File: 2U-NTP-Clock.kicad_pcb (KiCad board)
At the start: 2 copper layers, 482.6 x 83.8 mm, 279 parts, among them J1 Barrel_Jack_Switch, J2 Conn_01x06_Socket, Q1 BSS138, Q10 BSS138, Q11 BSS138, Q12 BSS138, Q13 BSS138, Q14 BSS138, Q15 BSS138, Q16 BSS138, Q17 BSS138, Q18 BSS138, Q19 BSS138, Q2 BSS138, Q20 BSS138, Q21 BSS138, Q22 BSS138, Q23 BSS138, Q24 BSS138, Q25 BSS138, Q26 BSS138, Q27 BSS138, Q28 BSS138, Q29 BSS138, Q3 BSS138, Q30 BSS138, Q31 BSS138, Q32 BSS138, Q33 BSS138, Q34 BSS138, Q35 BSS138, Q36 BSS138, Q37 BSS138, Q38 BSS138, Q39 BSS138, Q4 BSS138, Q40 BSS138, Q41 BSS138, Q42 BSS138, Q43 BSS138, Q5 BSS138, Q6 BSS138, Q7 BSS138, Q8 BSS138, Q9 BSS138, SW1 SW_Push, SW2 SW_Push, SW3 SW_Push, SW4 SW_Push, SW5 SW_Push, SW6 SW_Slide_DPDT, U3 74HC595, U4 74HC595, U5 74HC595, U6 74HC595, U7 74HC595, U8 74HC595, U9 L7805

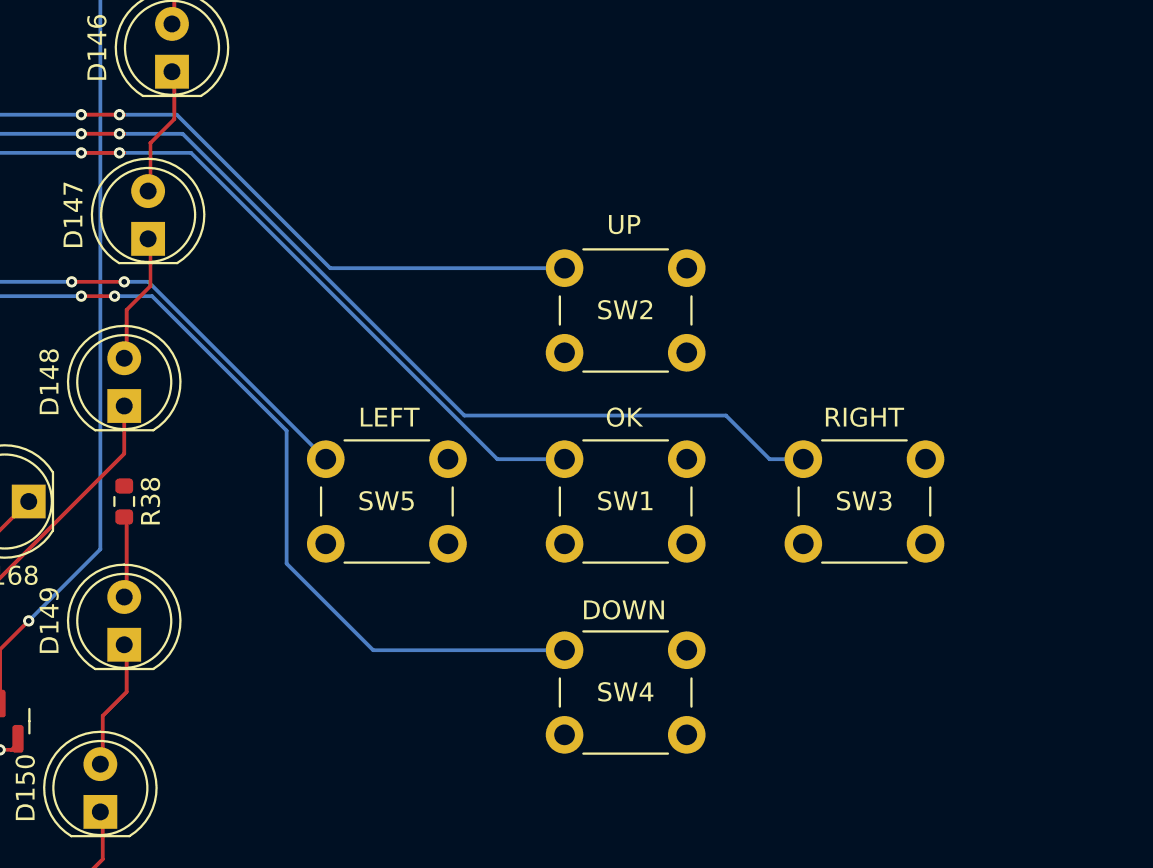
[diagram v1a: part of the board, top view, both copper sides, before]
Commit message: 操作用スイッチを移設
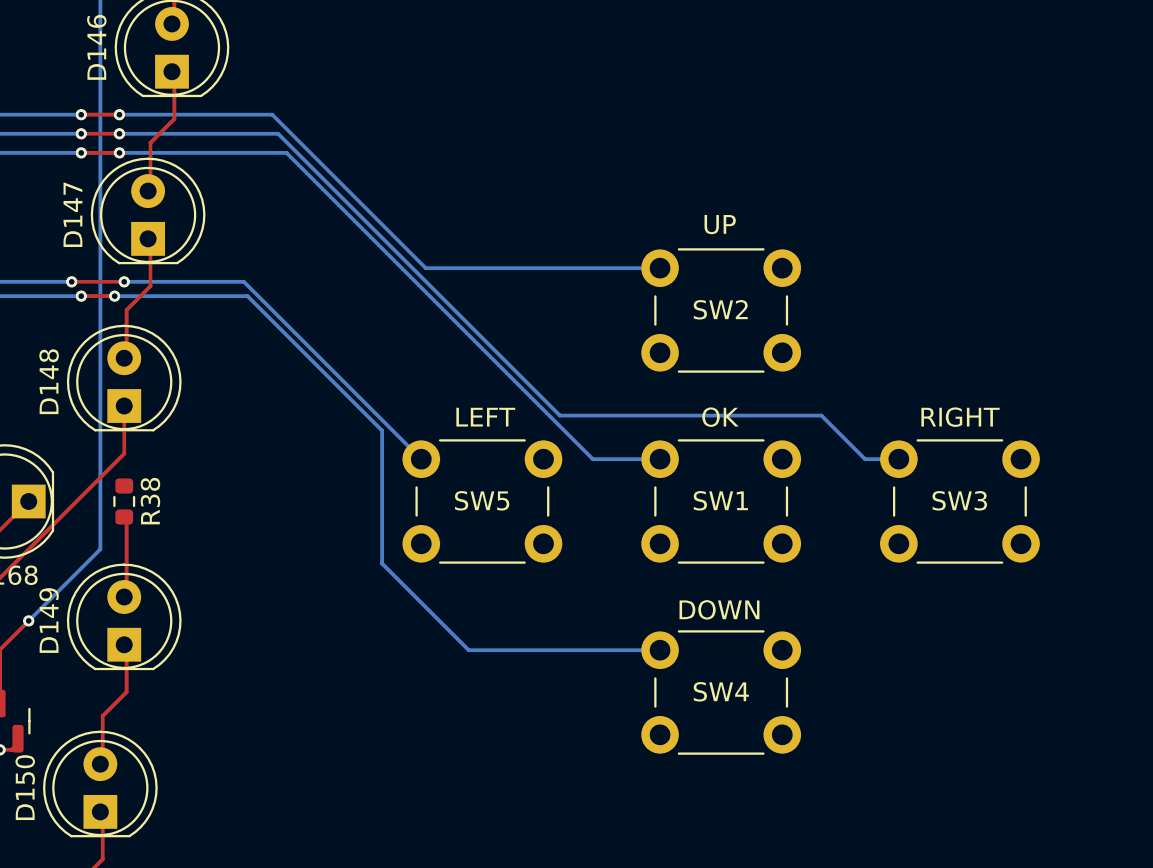
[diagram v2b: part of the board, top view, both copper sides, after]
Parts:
- moved SW1 5.08 mm to (499.7, 200.9)
- moved SW2 5.08 mm to (499.7, 190.8)
- moved SW4 5.08 mm to (499.7, 211.1)
- moved SW5 5.08 mm to (487.0, 200.9)
- moved SW3 5.08 mm to (512.4, 200.9)
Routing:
- net /UP: track 434.6 -> 439.7 mm
- net /RIGHT: track 449.6 -> 454.7 mm
- net /OK: track 434.9 -> 440.0 mm
- net /LEFT: track 404.9 -> 410.0 mm
- net /DOWN: track 421.8 -> 426.9 mm
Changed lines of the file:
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@@
 	(footprint "Button_Switch_THT:SW_PUSH_6mm"
 		(layer "F.Cu")
-		(at 481.89 200.95)
+		(at 486.97 200.95)
 		(descr "Generic 6mm SW tactile push button")
 		(tags "tact sw push 6mm")
@@
 	(footprint "Button_Switch_THT:SW_PUSH_6mm"
 		(layer "F.Cu")
-		(at 494.59 200.95)
+		(at 499.67 200.95)
 		(descr "Generic 6mm SW tactile push button")
 		(tags "tact sw push 6mm")
@@
 	(footprint "Button_Switch_THT:SW_PUSH_6mm"
 		(layer "F.Cu")
-		(at 494.59 190.79)
+		(at 499.67 190.79)
 		(descr "Generic 6mm SW tactile push button")
 		(tags "tact sw push 6mm")
@@
 	(footprint "Button_Switch_THT:SW_PUSH_6mm"
 		(layer "F.Cu")
-		(at 507.29 200.95)
+		(at 512.37 200.95)
 		(descr "Generic 6mm SW tactile push button")
 		(tags "tact sw push 6mm")
@@
 	(footprint "Button_Switch_THT:SW_PUSH_6mm"
 		(layer "F.Cu")
-		(at 494.59 211.11)
+		(at 499.67 211.11)
 		(descr "Generic 6mm SW tactile push button")
 		(tags "tact sw push 6mm")
@@
 	)
 	(gr_text "LEFT"
-		(at 485.25 198.75 0)
+		(at 490.33 198.75 0)
 		(layer "F.SilkS")
 		(effects
@@
 	)
 	(gr_text "DOWN"
-		(at 497.75 209 0)
+		(at 502.83 209 0)
 		(layer "F.SilkS")
 		(effects
@@
 	)
 	(gr_text "UP"
-		(at 497.75 188.5 0)
+		(at 502.83 188.5 0)
 		(layer "F.SilkS")
 		(effects
@@
 	)
 	(gr_text "OK"
-		(at 497.75 198.75 0)
+		(at 502.83 198.75 0)
 		(layer "F.SilkS")
 		(effects
@@
 	)
 	(gr_text "RIGHT"
-		(at 510.5 198.75 0)
+		(at 515.58 198.75 0)
 		(layer "F.SilkS")
 		(effects
@@
 	)
 	(segment
+		(start 479.806 184.658)
+		(end 496.098 200.95)
+		(width 0.2)
+		(layer "B.Cu")
+		(net 3)
+	)
+	(segment
 		(start 348.234 184.658)
 		(end 298.45 184.658)
@@
 	)
 	(segment
-		(start 474.726 184.658)
-		(end 471.17 184.658)
+		(start 471.17 184.658)
+		(end 479.806 184.658)
 		(width 0.2)
 		(layer "B.Cu")
@@
 	)
 	(segment
-		(start 491.018 200.95)
-		(end 474.726 184.658)
+		(start 247.396 181.102)
+		(end 242.824 181.102)
 		(width 0.2)
 		(layer "B.Cu")
@@
 	)
 	(segment
-		(start 247.396 181.102)
-		(end 242.824 181.102)
+		(start 104.902 221.234)
+		(end 104.902 218.636314)
 		(width 0.2)
 		(layer "B.Cu")
@@
 	)
 	(segment
-		(start 104.902 221.234)
-		(end 104.902 218.636314)
+		(start 496.098 200.95)
+		(end 499.67 200.95)
 		(width 0.2)
 		(layer "B.Cu")
@@
 	)
 	(segment
-		(start 494.59 200.95)
-		(end 491.018 200.95)
-		(width 0.2)
-		(layer "B.Cu")
-		(net 3)
-	)
-	(segment
 		(start 104.902 218.636314)
 		(end 106.622314 216.916)
@@
 	)
 	(segment
-		(start 473.964 182.626)
-		(end 471.17 182.626)
-		(width 0.2)
-		(layer "B.Cu")
-		(net 5)
-	)
-	(segment
 		(start 129.794 213.106)
 		(end 127 215.9)
@@
 	)
 	(segment
-		(start 494.59 190.79)
-		(end 482.128 190.79)
+		(start 471.17 182.626)
+		(end 479.044 182.626)
 		(width 0.2)
 		(layer "B.Cu")
@@
 	)
 	(segment
+		(start 487.208 190.79)
+		(end 499.67 190.79)
+		(width 0.2)
+		(layer "B.Cu")
+		(net 5)
+	)
+	(segment
 		(start 468.884 182.626)
 		(end 419.1 182.626)
@@
 	)
 	(segment
-		(start 482.128 190.79)
-		(end 473.964 182.626)
+		(start 479.044 182.626)
+		(end 487.208 190.79)
 		(width 0.2)
 		(layer "B.Cu")
@@
 	)
 	(segment
-		(start 507.29 200.95)
-		(end 505.496 200.95)
+		(start 510.576 200.95)
+		(end 512.37 200.95)
 		(width 0.2)
 		(layer "B.Cu")
@@
 	)
 	(segment
-		(start 104.502 218.332)
-		(end 104.502 222.104)
+		(start 508.254 198.628)
+		(end 510.576 200.95)
 		(width 0.2)
 		(layer "B.Cu")
@@
 	)
 	(segment
-		(start 505.496 200.95)
-		(end 503.174 198.628)
+		(start 104.502 218.332)
+		(end 104.502 222.104)
 		(width 0.2)
 		(layer "B.Cu")
@@
 	)
 	(segment
-		(start 503.174 198.628)
-		(end 489.261686 198.628)
+		(start 479.355686 183.642)
+		(end 494.341686 198.628)
 		(width 0.2)
 		(layer "B.Cu")
@@
 	)
 	(segment
-		(start 474.275686 183.642)
-		(end 471.17 183.642)
+		(start 358.648 183.642)
+		(end 350.52 183.642)
 		(width 0.2)
 		(layer "B.Cu")
@@
 	)
 	(segment
-		(start 358.648 183.642)
-		(end 350.52 183.642)
+		(start 130.302 189.992)
+		(end 130.302 213.36)
 		(width 0.2)
 		(layer "B.Cu")
@@
 	)
 	(segment
-		(start 489.261686 198.628)
-		(end 474.275686 183.642)
+		(start 468.884 183.642)
+		(end 419.1 183.642)
 		(width 0.2)
 		(layer "B.Cu")
@@
 	)
 	(segment
-		(start 130.302 189.992)
-		(end 130.302 213.36)
+		(start 471.17 183.642)
+		(end 479.355686 183.642)
 		(width 0.2)
 		(layer "B.Cu")
@@
 	)
 	(segment
-		(start 468.884 183.642)
-		(end 419.1 183.642)
+		(start 247.904 180.594)
+		(end 242.316 180.594)
 		(width 0.2)
 		(layer "B.Cu")
@@
 	)
 	(segment
-		(start 247.904 180.594)
-		(end 242.316 180.594)
+		(start 494.341686 198.628)
+		(end 508.254 198.628)
 		(width 0.2)
 		(layer "B.Cu")
@@
 	)
 	(segment
-		(start 484.414 211.11)
-		(end 479.806 206.502)
-		(width 0.2)
-		(layer "B.Cu")
-		(net 17)
-	)
-	(segment
 		(start 229.362 192.278)
 		(end 296.164 192.278)
@@
 	)
 	(segment
-		(start 131.826 197.104)
-		(end 136.652 192.278)
+		(start 470.662 192.278)
+		(end 477.732314 192.278)
 		(width 0.2)
 		(layer "B.Cu")
@@
 	)
 	(segment
-		(start 494.59 211.11)
-		(end 484.414 211.11)
+		(start 131.826 197.104)
+		(end 136.652 192.278)
 		(width 0.2)
 		(layer "B.Cu")
@@
 	)
 	(segment
-		(start 472.652314 192.278)
-		(end 470.662 192.278)
+		(start 484.886 199.431686)
+		(end 484.886 206.502)
 		(width 0.2)
 		(layer "B.Cu")
@@
 	)
 	(segment
-		(start 479.806 206.502)
-		(end 479.806 199.431686)
+		(start 477.732314 192.278)
+		(end 484.886 199.431686)
 		(width 0.2)
 		(layer "B.Cu")
@@
 	)
 	(segment
-		(start 479.806 199.431686)
-		(end 472.652314 192.278)
+		(start 489.494 211.11)
+		(end 499.67 211.11)
+		(width 0.2)
+		(layer "B.Cu")
+		(net 17)
+	)
+	(segment
+		(start 484.886 206.502)
+		(end 489.494 211.11)
 		(width 0.2)
 		(layer "B.Cu")
@@
 	)
 	(segment
-		(start 472.456 191.516)
-		(end 471.17 191.516)
+		(start 477.536 191.516)
+		(end 486.97 200.95)
 		(width 0.2)
 		(layer "B.Cu")
@@
 	)
 	(segment
-		(start 481.89 200.95)
-		(end 472.456 191.516)
+		(start 471.17 191.516)
+		(end 477.536 191.516)
 		(width 0.2)
 		(layer "B.Cu")

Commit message: 基板配線修正
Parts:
- moved R43 64.5 mm to (364.5, 164.1), turned to -90 degrees
- moved D170 40.6 mm to (364.5, 223.5), turned to 90 degrees
- moved D169 35.6 mm to (364.5, 185.4), turned to 90 degrees
- moved Q43 13.2 mm to (245.1, 241.8)
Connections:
- D103 pad 2: Net-(D102-K) -> Net-(D101-A)
- D104 pad 1: Net-(D104-K) -> Net-(D102-K)
- D107 pad 2: Net-(D106-K) -> Net-(D105-A)
- D108 pad 1: Net-(D108-K) -> Net-(D106-K)
- D11 pad 2: Net-(D10-K) -> Net-(D11-A)
- D111 pad 2: Net-(D110-K) -> Net-(D109-A)
- D112 pad 1: Net-(D112-K) -> Net-(D110-K)
- D115 pad 2: Net-(D114-K) -> Net-(D113-A)
- D116 pad 1: Net-(D116-K) -> Net-(D114-K)
- D119 pad 2: Net-(D118-K) -> Net-(D117-A)
- D12 pad 1: Net-(D12-K) -> Net-(D10-K)
- D120 pad 1: Net-(D120-K) -> Net-(D118-K)
- D123 pad 2: Net-(D122-K) -> Net-(D121-A)
- D124 pad 1: Net-(D124-K) -> Net-(D122-K)
- D127 pad 2: Net-(D126-K) -> Net-(D125-A)
- D128 pad 1: Net-(D128-K) -> Net-(D126-K)
- D131 pad 2: Net-(D130-K) -> Net-(D129-A)
- D132 pad 1: Net-(D132-K) -> Net-(D130-K)
- D135 pad 2: Net-(D134-K) -> Net-(D133-A)
- D136 pad 1: Net-(D136-K) -> Net-(D134-K)
- D139 pad 2: Net-(D138-K) -> Net-(D137-A)
- D140 pad 1: Net-(D140-K) -> Net-(D138-K)
- D143 pad 2: Net-(D142-K) -> Net-(D141-A)
- D144 pad 1: Net-(D144-K) -> Net-(D142-K)
- D147 pad 2: Net-(D146-K) -> Net-(D145-A)
- D148 pad 1: Net-(D148-K) -> Net-(D146-K)
- D15 pad 2: Net-(D14-K) -> Net-(D13-A)
- D151 pad 2: Net-(D150-K) -> Net-(D149-A)
- D152 pad 1: Net-(D152-K) -> Net-(D150-K)
- D155 pad 2: Net-(D154-K) -> Net-(D153-A)
- D156 pad 1: Net-(D156-K) -> Net-(D154-K)
- D159 pad 2: Net-(D158-K) -> Net-(D157-A)
- D16 pad 1: Net-(D16-K) -> Net-(D14-K)
- D160 pad 1: Net-(D160-K) -> Net-(D158-K)
- D163 pad 2: Net-(D162-K) -> Net-(D161-A)
- D164 pad 1: Net-(D164-K) -> Net-(D162-K)
- D167 pad 2: Net-(D166-K) -> Net-(D165-A)
- D168 pad 1: Net-(D168-K) -> Net-(D166-K)
- D171 pad 2: Net-(D170-K) -> Net-(D169-A)
- D172 pad 1: Net-(D172-K) -> Net-(D170-K)
- D19 pad 2: Net-(D18-K) -> Net-(D17-A)
- D20 pad 1: Net-(D20-K) -> Net-(D18-K)
- D23 pad 2: Net-(D22-K) -> Net-(D21-A)
- D24 pad 1: Net-(D24-K) -> Net-(D22-K)
- D27 pad 2: Net-(D26-K) -> Net-(D25-A)
- D28 pad 1: Net-(D28-K) -> Net-(D26-K)
- D3 pad 2: Net-(D2-K) -> Net-(D1-A)
- D31 pad 2: Net-(D30-K) -> Net-(D29-A)
- D32 pad 1: Net-(D32-K) -> Net-(D30-K)
- D35 pad 2: Net-(D34-K) -> Net-(D33-A)
- D36 pad 1: Net-(D36-K) -> Net-(D34-K)
- D39 pad 2: Net-(D38-K) -> Net-(D37-A)
- D4 pad 1: Net-(D4-K) -> Net-(D2-K)
- D40 pad 1: Net-(D40-K) -> Net-(D38-K)
- D43 pad 2: Net-(D42-K) -> Net-(D41-A)
- D44 pad 1: Net-(D44-K) -> Net-(D42-K)
- D47 pad 2: Net-(D46-K) -> Net-(D45-A)
- D48 pad 1: Net-(D48-K) -> Net-(D46-K)
- D51 pad 2: Net-(D50-K) -> Net-(D49-A)
- D52 pad 1: Net-(D52-K) -> Net-(D50-K)
- D55 pad 2: Net-(D54-K) -> Net-(D53-A)
- D56 pad 1: Net-(D56-K) -> Net-(D54-K)
- D59 pad 2: Net-(D58-K) -> Net-(D57-A)
- D60 pad 1: Net-(D60-K) -> Net-(D58-K)
- D63 pad 2: Net-(D62-K) -> Net-(D61-A)
- D64 pad 1: Net-(D64-K) -> Net-(D62-K)
- D67 pad 2: Net-(D66-K) -> Net-(D65-A)
- D68 pad 1: Net-(D68-K) -> Net-(D66-K)
- D7 pad 2: Net-(D6-K) -> Net-(D5-A)
- D71 pad 2: Net-(D70-K) -> Net-(D69-A)
- D72 pad 1: Net-(D72-K) -> Net-(D70-K)
- D75 pad 2: Net-(D74-K) -> Net-(D73-A)
- D76 pad 1: Net-(D76-K) -> Net-(D74-K)
- D79 pad 2: Net-(D78-K) -> Net-(D77-A)
- D8 pad 1: Net-(D8-K) -> Net-(D6-K)
- D80 pad 1: Net-(D80-K) -> Net-(D78-K)
- D83 pad 2: Net-(D82-K) -> Net-(D81-A)
- D84 pad 1: Net-(D84-K) -> Net-(D82-K)
- D87 pad 2: Net-(D86-K) -> Net-(D85-A)
- D88 pad 1: Net-(D88-K) -> Net-(D86-K)
- D9 pad 2: Net-(D9-A) -> Net-(D11-A)
- D91 pad 2: Net-(D90-K) -> Net-(D89-A)
- D92 pad 1: Net-(D92-K) -> Net-(D90-K)
- D95 pad 2: Net-(D94-K) -> Net-(D93-A)
- D96 pad 1: Net-(D96-K) -> Net-(D94-K)
- D98 pad 1: Net-(D98-K) -> Net-(D100-K)
- D99 pad 2: Net-(D98-K) -> Net-(D97-A)
- Q1 pad 3: Net-(D4-K) -> Net-(D2-K)
- Q10 pad 3: Net-(D40-K) -> Net-(D38-K)
- Q11 pad 3: Net-(D44-K) -> Net-(D42-K)
- Q12 pad 3: Net-(D48-K) -> Net-(D46-K)
- Q13 pad 3: Net-(D52-K) -> Net-(D50-K)
- Q14 pad 3: Net-(D56-K) -> Net-(D54-K)
- Q15 pad 3: Net-(D60-K) -> Net-(D58-K)
- Q16 pad 3: Net-(D64-K) -> Net-(D62-K)
- Q17 pad 3: Net-(D68-K) -> Net-(D66-K)
- Q18 pad 3: Net-(D72-K) -> Net-(D70-K)
- Q19 pad 3: Net-(D76-K) -> Net-(D74-K)
- Q2 pad 3: Net-(D8-K) -> Net-(D6-K)
- Q20 pad 3: Net-(D80-K) -> Net-(D78-K)
- Q21 pad 3: Net-(D84-K) -> Net-(D82-K)
- Q22 pad 3: Net-(D88-K) -> Net-(D86-K)
- Q23 pad 3: Net-(D92-K) -> Net-(D90-K)
- Q24 pad 3: Net-(D96-K) -> Net-(D94-K)
- Q26 pad 3: Net-(D104-K) -> Net-(D102-K)
- Q27 pad 3: Net-(D108-K) -> Net-(D106-K)
- Q28 pad 3: Net-(D112-K) -> Net-(D110-K)
- Q29 pad 3: Net-(D116-K) -> Net-(D114-K)
- Q3 pad 3: Net-(D12-K) -> Net-(D10-K)
- Q30 pad 3: Net-(D120-K) -> Net-(D118-K)
- Q31 pad 3: Net-(D124-K) -> Net-(D122-K)
- Q32 pad 3: Net-(D128-K) -> Net-(D126-K)
- Q33 pad 3: Net-(D132-K) -> Net-(D130-K)
- Q34 pad 3: Net-(D136-K) -> Net-(D134-K)
- Q35 pad 3: Net-(D140-K) -> Net-(D138-K)
- Q36 pad 3: Net-(D144-K) -> Net-(D142-K)
- Q37 pad 3: Net-(D148-K) -> Net-(D146-K)
- Q38 pad 3: Net-(D152-K) -> Net-(D150-K)
- Q39 pad 3: Net-(D156-K) -> Net-(D154-K)
- Q4 pad 3: Net-(D16-K) -> Net-(D14-K)
- Q40 pad 3: Net-(D160-K) -> Net-(D158-K)
- Q41 pad 3: Net-(D164-K) -> Net-(D162-K)
- Q42 pad 3: Net-(D168-K) -> Net-(D166-K)
- Q43 pad 3: Net-(D172-K) -> Net-(D170-K)
- Q5 pad 3: Net-(D20-K) -> Net-(D18-K)
- Q6 pad 3: Net-(D24-K) -> Net-(D22-K)
- Q7 pad 3: Net-(D28-K) -> Net-(D26-K)
- Q8 pad 3: Net-(D32-K) -> Net-(D30-K)
- Q9 pad 3: Net-(D36-K) -> Net-(D34-K)
- R3 pad 2: Net-(D9-A) -> Net-(D11-A)
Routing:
- net Net-(D169-A): track 4.25 -> 157.2 mm
- net Net-(D114-K): track 6.35 -> 69.9 mm, vias 0 -> 1
- net Net-(D142-K): track 6.35 -> 69.8 mm, vias 0 -> 1
- net Net-(D2-K): track 6.35 -> 69.8 mm, vias 0 -> 1
- net Net-(D30-K): track 6.35 -> 69.8 mm, vias 0 -> 1
- net Net-(D58-K): track 6.35 -> 69.8 mm, vias 0 -> 1
- net Net-(D86-K): track 6.35 -> 69.8 mm, vias 0 -> 1
- net Net-(D116-K): track 51.1 -> 0.00 mm, vias 1 -> 0
- net Net-(D144-K): track 51.1 -> 0.00 mm, vias 1 -> 0
- net Net-(D4-K): track 51.0 -> 0.00 mm, vias 1 -> 0
- net Net-(D88-K): track 51.0 -> 0.00 mm, vias 1 -> 0
- net Net-(D60-K): track 51.0 -> 0.00 mm, vias 1 -> 0
- net Net-(D32-K): track 51.0 -> 0.00 mm, vias 1 -> 0
- net Net-(D26-K): track 6.35 -> 54.2 mm
- net Net-(D166-K): track 6.35 -> 52.4 mm
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
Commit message: スイッチ位置変更
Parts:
- moved SW1 2.08 mm to (497.6, 200.9)
- moved SW2 2.08 mm to (497.6, 190.8)
- moved SW3 2.08 mm to (510.3, 200.9)
- moved SW4 2.08 mm to (497.6, 211.1)
- moved SW5 2.08 mm to (484.9, 200.9)
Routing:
- net /OK: track 440.0 -> 464.5 mm
- net /RIGHT: track 454.7 -> 478.0 mm
- net /UP: track 439.7 -> 450.1 mm
- net /DOWN: track 426.9 -> 431.8 mm
- net /LEFT: track 410.0 -> 407.9 mm
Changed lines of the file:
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@@
 	(footprint "Button_Switch_THT:SW_PUSH_6mm"
 		(layer "F.Cu")
-		(at 486.97 200.95)
+		(at 484.886 200.95)
 		(descr "Generic 6mm SW tactile push button")
 		(tags "tact sw push 6mm")
@@
 	(footprint "Button_Switch_THT:SW_PUSH_6mm"
 		(layer "F.Cu")
-		(at 499.67 200.95)
+		(at 497.586 200.95)
 		(descr "Generic 6mm SW tactile push button")
 		(tags "tact sw push 6mm")
@@
 	(footprint "Button_Switch_THT:SW_PUSH_6mm"
 		(layer "F.Cu")
-		(at 499.67 190.79)
+		(at 497.586 190.79)
 		(descr "Generic 6mm SW tactile push button")
 		(tags "tact sw push 6mm")
@@
 		)
 		(property "Value" "LED"
-			(at 1.27 3.96 90)
+			(at 1.27 6.956 90)
 			(layer "F.Fab")
 			(effects
@@
 	(footprint "Button_Switch_THT:SW_PUSH_6mm"
 		(layer "F.Cu")
-		(at 512.37 200.95)
+		(at 510.286 200.95)
 		(descr "Generic 6mm SW tactile push button")
 		(tags "tact sw push 6mm")
@@
 	(footprint "Button_Switch_THT:SW_PUSH_6mm"
 		(layer "F.Cu")
-		(at 499.67 211.11)
+		(at 497.586 211.11)
 		(descr "Generic 6mm SW tactile push button")
 		(tags "tact sw push 6mm")
@@
 	)
 	(gr_text "LEFT"
-		(at 490.33 198.75 0)
+		(at 488.246 198.75 0)
 		(layer "F.SilkS")
 		(effects
@@
 	)
 	(gr_text "DOWN"
-		(at 502.83 209 0)
+		(at 500.746 209 0)
 		(layer "F.SilkS")
 		(effects
@@
 	)
 	(gr_text "UP"
-		(at 502.83 188.5 0)
+		(at 500.746 188.5 0)
 		(layer "F.SilkS")
 		(effects
@@
 	)
 	(gr_text "OK"
-		(at 502.83 198.75 0)
+		(at 500.746 198.75 0)
 		(layer "F.SilkS")
 		(effects
@@
 	)
 	(gr_text "RIGHT"
-		(at 515.58 198.75 0)
+		(at 513.496 198.75 0)
 		(layer "F.SilkS")
 		(effects
@@
 	)
 	(segment
+		(start 477.722 184.658)
+		(end 494.014 200.95)
+		(width 0.2)
+		(layer "B.Cu")
+		(net 3)
+	)
+	(segment
 		(start 471.17 184.658)
-		(end 479.806 184.658)
+		(end 477.722 184.658)
+		(width 0.2)
+		(layer "B.Cu")
+		(net 3)
+	)
+	(segment
+		(start 494.014 200.95)
+		(end 497.586 200.95)
 		(width 0.2)
 		(layer "B.Cu")
@@
 	)
 	(segment
+		(start 471.17 182.626)
+		(end 476.96 182.626)
+		(width 0.2)
+		(layer "B.Cu")
+		(net 5)
+	)
+	(segment
 		(start 104.102 218.166314)
 		(end 104.102 222.974)
@@
 	)
 	(segment
-		(start 471.17 182.626)
-		(end 479.044 182.626)
+		(start 485.124 190.79)
+		(end 497.586 190.79)
 		(width 0.2)
 		(layer "B.Cu")
@@
 	)
 	(segment
-		(start 416.814 182.626)
-		(end 370.332 182.626)
+		(start 476.96 182.626)
+		(end 485.124 190.79)
 		(width 0.2)
 		(layer "B.Cu")
@@
 	)
 	(segment
-		(start 227.584 182.626)
-		(end 177.8 182.626)
+		(start 416.814 182.626)
+		(end 370.332 182.626)
 		(width 0.2)
 		(layer "B.Cu")
@@
 	)
 	(segment
-		(start 479.044 182.626)
-		(end 487.208 190.79)
+		(start 227.584 182.626)
+		(end 177.8 182.626)
 		(width 0.2)
 		(layer "B.Cu")
@@
 	)
 	(segment
-		(start 510.576 200.95)
-		(end 512.37 200.95)
-		(width 0.2)
-		(layer "B.Cu")
-		(net 14)
-	)
-	(segment
 		(start 127.254 216.408)
 		(end 106.426 216.408)
@@
 	)
 	(segment
-		(start 479.355686 183.642)
-		(end 494.341686 198.628)
-		(width 0.2)
-		(layer "B.Cu")
-		(net 14)
-	)
-	(segment
 		(start 361.696 180.594)
 		(end 358.648 183.642)
@@
 	)
 	(segment
+		(start 506.17 198.628)
+		(end 508.492 200.95)
+		(width 0.2)
+		(layer "B.Cu")
+		(net 14)
+	)
+	(segment
 		(start 416.814 183.642)
 		(end 370.332 183.642)
@@
 	)
 	(segment
+		(start 508.492 200.95)
+		(end 510.286 200.95)
+		(width 0.2)
+		(layer "B.Cu")
+		(net 14)
+	)
+	(segment
 		(start 136.652 183.642)
 		(end 130.302 189.992)
@@
 	)
 	(segment
+		(start 492.257686 198.628)
+		(end 506.17 198.628)
+		(width 0.2)
+		(layer "B.Cu")
+		(net 14)
+	)
+	(segment
 		(start 250.952 183.642)
 		(end 247.904 180.594)
@@
 	)
 	(segment
+		(start 471.17 183.642)
+		(end 477.271686 183.642)
+		(width 0.2)
+		(layer "B.Cu")
+		(net 14)
+	)
+	(segment
+		(start 477.271686 183.642)
+		(end 492.257686 198.628)
+		(width 0.2)
+		(layer "B.Cu")
+		(net 14)
+	)
+	(segment
 		(start 367.284 180.594)
 		(end 361.696 180.594)
@@
 	)
 	(segment
+		(start 470.662 192.278)
+		(end 475.648314 192.278)
+		(width 0.2)
+		(layer "B.Cu")
+		(net 17)
+	)
+	(segment
 		(start 106.68 219.709995)
 		(end 106.68 218.694)
@@
 	)
 	(segment
+		(start 482.802 199.431686)
+		(end 482.802 206.502)
+		(width 0.2)
+		(layer "B.Cu")
+		(net 17)
+	)
+	(segment
 		(start 229.362 192.278)
 		(end 296.164 192.278)
@@
 	)
 	(segment
-		(start 177.292 192.278)
-		(end 227.584 192.278)
+		(start 487.41 211.11)
+		(end 497.586 211.11)
 		(width 0.2)
 		(layer "B.Cu")
@@
 	)
 	(segment
-		(start 350.012 192.278)
-		(end 416.814 192.278)
+		(start 177.292 192.278)
+		(end 227.584 192.278)
 		(width 0.2)
 		(layer "B.Cu")
@@
 	)
 	(segment
-		(start 484.886 199.431686)
-		(end 484.886 206.502)
+		(start 350.012 192.278)
+		(end 416.814 192.278)
 		(width 0.2)
 		(layer "B.Cu")
@@
 	)
 	(segment
-		(start 477.732314 192.278)
-		(end 484.886 199.431686)
-		(width 0.2)
-		(layer "B.Cu")
-		(net 17)
-	)
-	(segment
 		(start 131.826 214.122)
 		(end 131.826 197.104)
@@
 	)
 	(segment
-		(start 489.494 211.11)
-		(end 499.67 211.11)
+		(start 482.802 206.502)
+		(end 487.41 211.11)
 		(width 0.2)
 		(layer "B.Cu")
@@
 	)
 	(segment
-		(start 484.886 206.502)
-		(end 489.494 211.11)
+		(start 475.648314 192.278)
+		(end 482.802 199.431686)
 		(width 0.2)
 		(layer "B.Cu")
@@
 	)
 	(segment
-		(start 105.41 220.472)
-		(end 105.917998 220.979998)
+		(start 471.17 191.516)
+		(end 475.452 191.516)
 		(width 0.2)
 		(layer "B.Cu")
@@
 	)
 	(segment
-		(start 477.536 191.516)
-		(end 486.97 200.95)
+		(start 105.41 220.472)
+		(end 105.917998 220.979998)
 		(width 0.2)
 		(layer "B.Cu")
@@
 	)
 	(segment
+		(start 475.452 191.516)
+		(end 484.886 200.95)
+		(width 0.2)
+		(layer "B.Cu")
+		(net 18)
+	)
+	(segment
 		(start 136.652 191.516)
 		(end 131.318 196.85)
@@
 		(width 0.2)
 		(layer "B.Cu")
-		(net 18)
-	)
-	(segment
-		(start 471.17 191.516)
-		(end 477.536 191.516)
-		(width 0.2)
-		(layer "B.Cu")
